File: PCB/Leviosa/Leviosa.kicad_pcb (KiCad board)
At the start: 2 copper layers, 80 x 80 mm, 26 parts, among them Q3 TIP122, Q4 TIP122, U1 LM324, U2 ATtiny13A-P, U3 TPS1H200AQDGNRQ1, U5 L7805, U6 SS495A

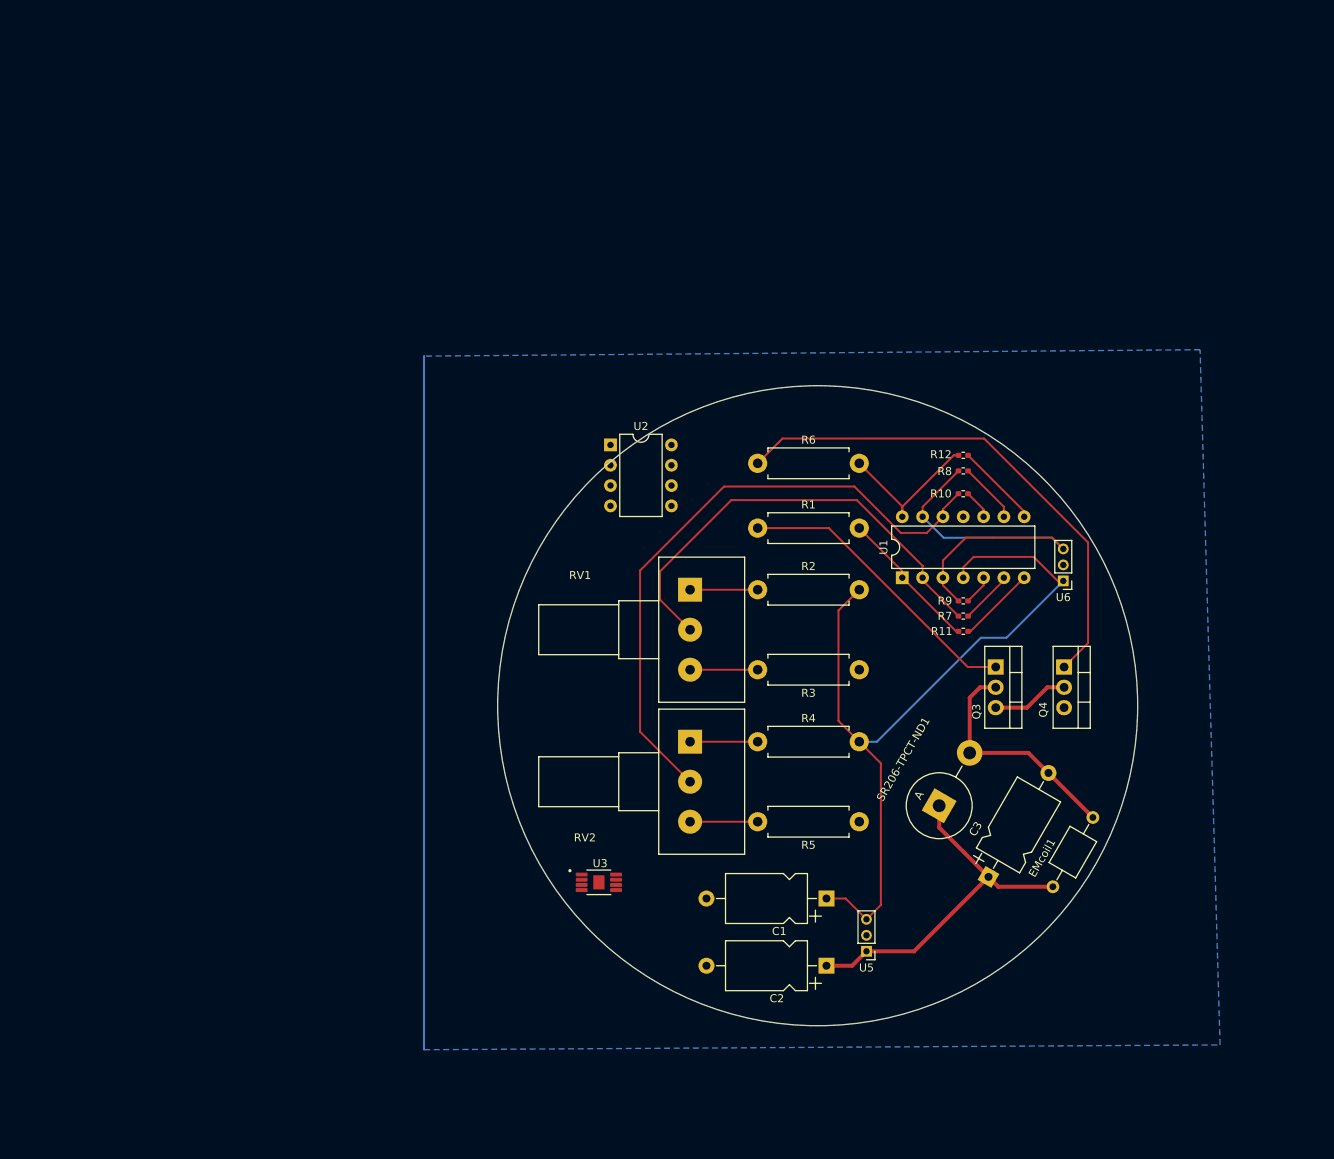
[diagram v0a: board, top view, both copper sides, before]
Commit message: update schematic footprints. PCB is sad now
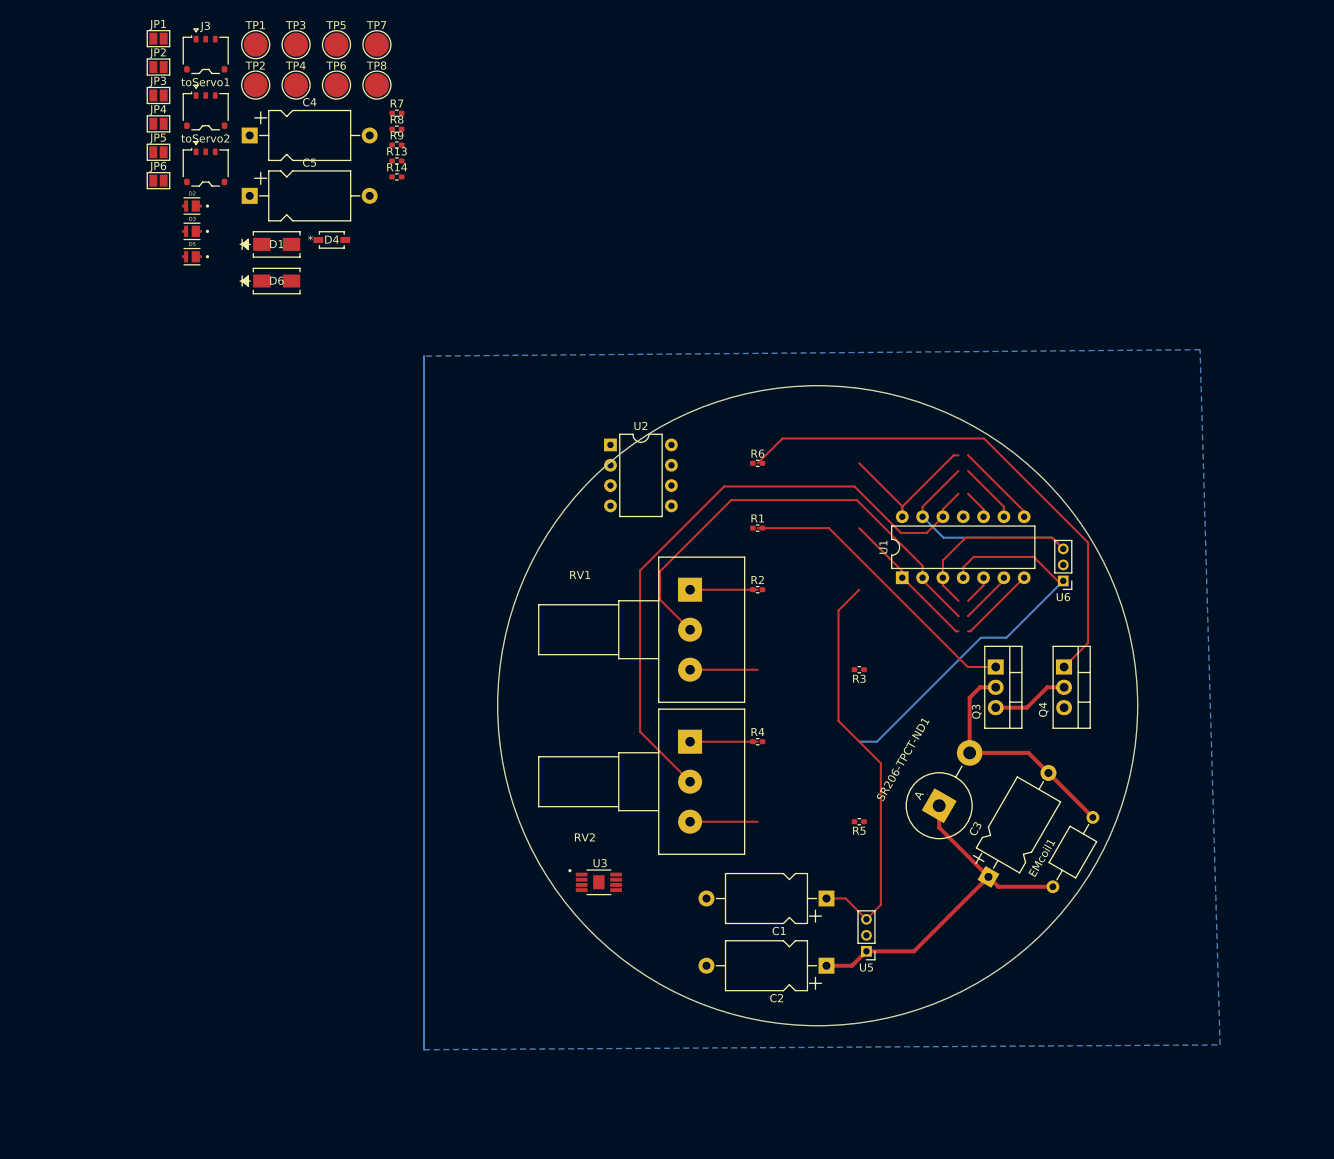
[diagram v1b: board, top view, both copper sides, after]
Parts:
- removed R10, R11, R12: DNP, Resistor_SMD:R_0402_1005Metric_Pad0.72x0.64mm_HandSolder
- added C4: 10µF, Capacitor_THT:CP_Axial_L10.0mm_D6.0mm_P15.00mm_Horizontal, F.Cu at (94.0, 42.7)
- added C5: 10µF, Capacitor_THT:CP_Axial_L10.0mm_D6.0mm_P15.00mm_Horizontal, F.Cu at (94.0, 50.3)
- added D1: D_Zener, SMAZ9V1-13-F:SMA_DIO, F.Cu at (97.4, 56.3)
- added D2: LED, MP-2016-1100-50-70:LED_MP-2016-1100-50-70, F.Cu at (86.8, 51.5)
- added D3: LED, MP-2016-1100-50-70:LED_MP-2016-1100-50-70, F.Cu at (86.8, 54.7)
- added D4: D_Zener, SZMMSZ4679T1G:SOD-123_ONS, F.Cu at (104.3, 55.8)
- added D5: LED, MP-2016-1100-50-70:LED_MP-2016-1100-50-70, F.Cu at (86.8, 57.9)
- added D6: D_Zener, SMAZ9V1-13-F:SMA_DIO, F.Cu at (97.4, 60.9)
- added J3: Conn_01x03, Connector_JST:JST_ACH_BM03B-ACHSS-GAN-ETF_1x03-1MP_P1.20mm_Vertical, F.Cu at (88.5, 32.6)
- added JP1: SolderJumper_2_Open, Jumper:SolderJumper-2_P1.3mm_Open_Pad1.0x1.5mm, F.Cu at (82.6, 30.6)
- added JP2: SolderJumper_2_Open, Jumper:SolderJumper-2_P1.3mm_Open_Pad1.0x1.5mm, F.Cu at (82.6, 34.2)
- added JP3: SolderJumper_2_Open, Jumper:SolderJumper-2_P1.3mm_Open_Pad1.0x1.5mm, F.Cu at (82.6, 37.7)
- added JP4: SolderJumper_2_Open, Jumper:SolderJumper-2_P1.3mm_Open_Pad1.0x1.5mm, F.Cu at (82.6, 41.3)
- added JP5: SolderJumper_2_Open, Jumper:SolderJumper-2_P1.3mm_Open_Pad1.0x1.5mm, F.Cu at (82.6, 44.8)
- added JP6: SolderJumper_2_Open, Jumper:SolderJumper-2_P1.3mm_Open_Pad1.0x1.5mm, F.Cu at (82.6, 48.4)
- added R13: 8kΩ, Resistor_SMD:R_0402_1005Metric_Pad0.72x0.64mm_HandSolder, F.Cu at (112.4, 45.9)
- added R14: 100kΩ, Resistor_SMD:R_0402_1005Metric_Pad0.72x0.64mm_HandSolder, F.Cu at (112.4, 47.9)
- added TP1: TestPoint, TestPoint:TestPoint_Pad_D3.0mm, F.Cu at (94.8, 31.4)
- added TP2: TestPoint, TestPoint:TestPoint_Pad_D3.0mm, F.Cu at (94.8, 36.4)
- added TP3: TestPoint, TestPoint:TestPoint_Pad_D3.0mm, F.Cu at (99.8, 31.4)
- added TP4: TestPoint, TestPoint:TestPoint_Pad_D3.0mm, F.Cu at (99.8, 36.4)
- added TP5: TestPoint, TestPoint:TestPoint_Pad_D3.0mm, F.Cu at (104.9, 31.4)
- added TP6: TestPoint, TestPoint:TestPoint_Pad_D3.0mm, F.Cu at (104.9, 36.4)
- added TP7: TestPoint, TestPoint:TestPoint_Pad_D3.0mm, F.Cu at (109.9, 31.4)
- added TP8: TestPoint, TestPoint:TestPoint_Pad_D3.0mm, F.Cu at (109.9, 36.4)
- added toServo1: Conn_01x03, Connector_JST:JST_ACH_BM03B-ACHSS-GAN-ETF_1x03-1MP_P1.20mm_Vertical, F.Cu at (88.5, 39.6)
- added toServo2: Conn_01x03, Connector_JST:JST_ACH_BM03B-ACHSS-GAN-ETF_1x03-1MP_P1.20mm_Vertical, F.Cu at (88.5, 46.6)
- C1: value 10µF -> 0.1µF
- C2: value 10µF -> 0.33µF
- R1, R4, R5, R6: footprint Resistor_THT:R_Axial_DIN0411_L9.9mm_D3.6mm_P12.70mm_Horizontal -> Resistor_SMD:R_0402_1005Metric_Pad0.72x0.64mm_HandSolder
- R2: value 200kΩ -> 100kΩ; footprint Resistor_THT:R_Axial_DIN0411_L9.9mm_D3.6mm_P12.70mm_Horizontal -> Resistor_SMD:R_0402_1005Metric_Pad0.72x0.64mm_HandSolder
- R3: value 27kΩ -> 7.8kΩ; footprint Resistor_THT:R_Axial_DIN0411_L9.9mm_D3.6mm_P12.70mm_Horizontal -> Resistor_SMD:R_0402_1005Metric_Pad0.72x0.64mm_HandSolder
- R7, R8, R9: value DNP -> 1kΩ
- moved R7 94.7 mm to (112.4, 39.9), turned to 0 degrees
- moved R9 90.9 mm to (112.4, 43.9), turned to 0 degrees
- moved R8 82.7 mm to (112.4, 41.9)
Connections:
- C3 pad 1: +12V -> /V_out
- EMcoil1 pad 1: +12V -> /V_out
- R7 pad 1: Net-(U1B--) -> Net-(D2-K)
- R7 pad 2: /set_point -> GND
- R8 pad 1: /hall_output -> Net-(D3-K)
- R8 pad 2: Net-(U1C--) -> GND
- R9 pad 1: Net-(U1B-+) -> Net-(D5-K)
- R9 pad 2: /hall_output -> GND
- RV1 pad 1: Net-(R2-Pad1) -> Net-(R3-Pad2)
- RV1 pad 3: Net-(R3-Pad2) -> Net-(R2-Pad1)
- SR206-TPCT-ND1 pad 1: +12V -> /V_out
- U1 pad 5: Net-(U1B-+) -> Net-(JP3-B)
- U1 pad 6: Net-(U1B--) -> Net-(JP4-B)
- U1 pad 9: Net-(U1C--) -> Net-(JP5-A)
- U2 pad 1: unconnected-(U2-~{RESET}/PB5-Pad1) -> Net-(J3-Pin_3)
- U2 pad 2: unconnected-(U2-PB3-Pad2) -> Net-(J3-Pin_1)
- U2 pad 3: unconnected-(U2-PB4-Pad3) -> Net-(J3-Pin_2)
- U2 pad 4: unconnected-(U2-GND-Pad4) -> GND
- U2 pad 5: unconnected-(U2-PB0-Pad5) -> Net-(U2-PB0)
- U2 pad 6: unconnected-(U2-PB1-Pad6) -> Net-(U2-PB1)
- U2 pad 7: unconnected-(U2-PB2-Pad7) -> /hall_output
- U2 pad 8: unconnected-(U2-VCC-Pad8) -> /5V
- U3 pad 1: unconnected-(U3-IN-Pad1) -> +12V
- U3 pad 2: unconnected-(U3-DIAG_EN-Pad2) -> +12V
- U3 pad 3: unconnected-(U3-~{FAULT}-Pad3) -> Net-(U3-~{FAULT})
- U3 pad 4: unconnected-(U3-CL-Pad4) -> Net-(U3-CL)
- U3 pad 5: unconnected-(U3-DELAY-Pad5) -> Net-(U3-DELAY)
- U3 pad 6: unconnected-(U3-GND-Pad6) -> GND
- U3 pad 7: unconnected-(U3-OUT-Pad7) -> /V_out
- U3 pad 8: unconnected-(U3-VS-Pad8) -> +12V
- U3 pad 9: unconnected-(U3-EP-Pad9) -> GND
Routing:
- net Net-(R3-Pad2): track 8.45 -> 0.00 mm
- net Net-(R2-Pad1): track 8.45 -> 16.9 mm
- net Net-(U1C--): track 7.58 -> 0.00 mm
- net Net-(JP5-A): track 0.00 -> 7.58 mm
- net Net-(U1B--): track 6.66 -> 0.00 mm
- net Net-(JP4-B): track 0.00 -> 6.66 mm
- net Net-(U1B-+): track 3.70 -> 0.00 mm
- net Net-(JP3-B): track 0.00 -> 3.70 mm

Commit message: update footprints and the like
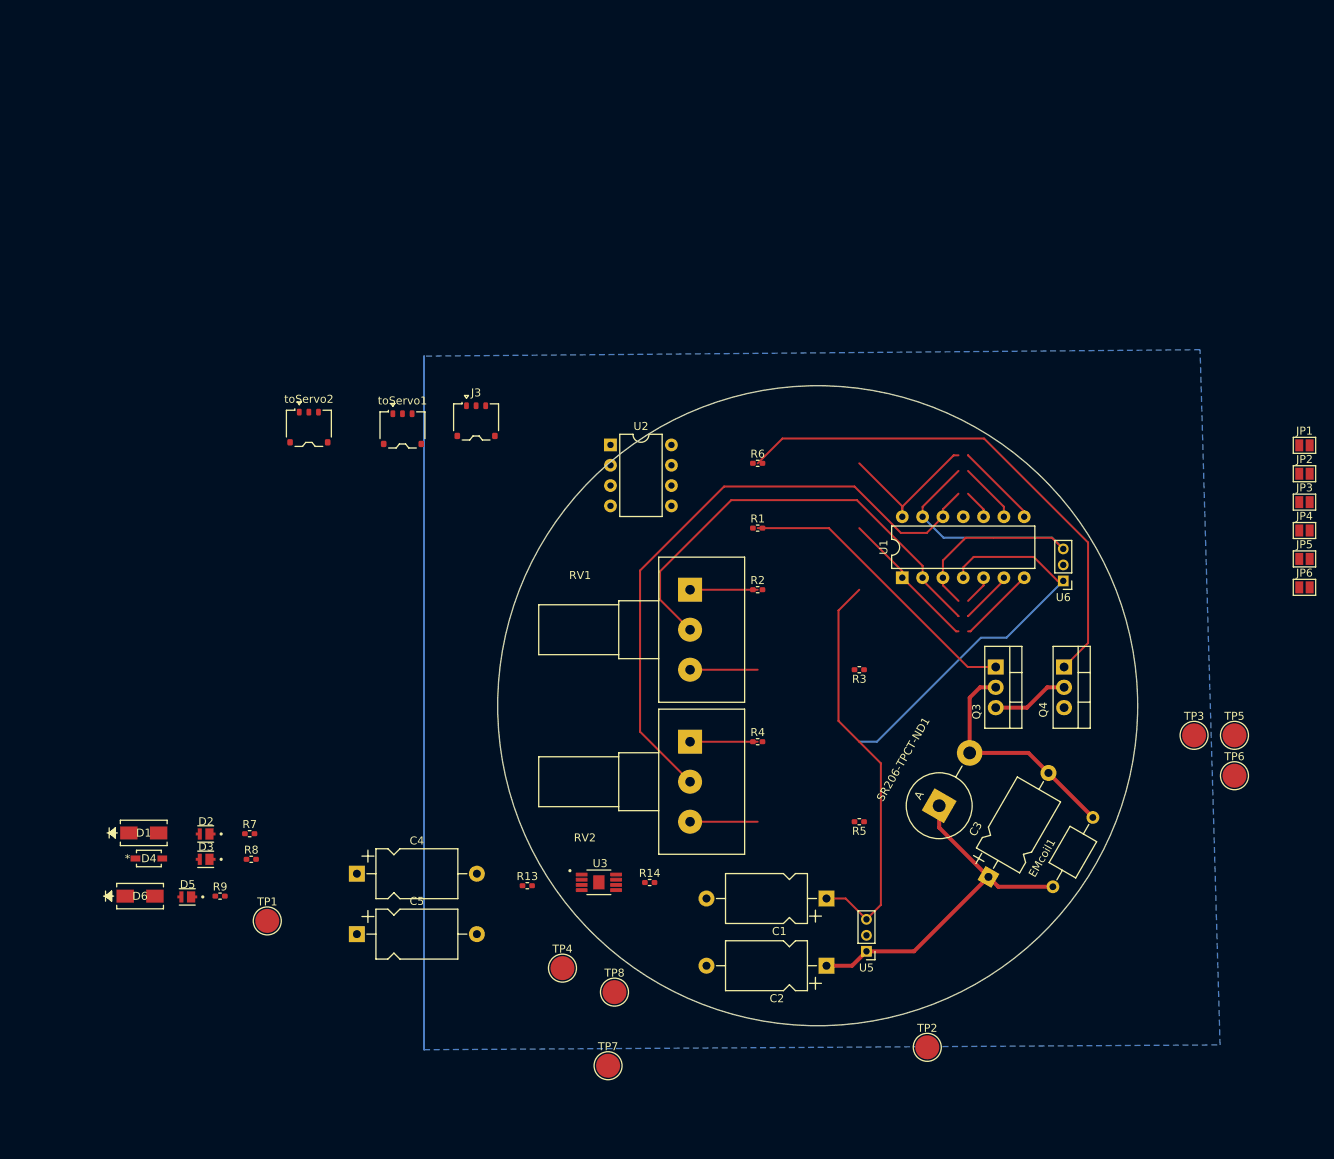
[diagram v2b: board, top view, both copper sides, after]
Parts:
- moved JP1 152.0 mm to (225.8, 81.5)
- moved JP2 152.0 mm to (225.8, 85.0)
- moved JP3 152.0 mm to (225.8, 88.5)
- moved JP4 152.0 mm to (225.8, 92.1)
- moved JP5 152.0 mm to (225.8, 95.7)
- moved JP6 152.0 mm to (225.8, 99.2)
- moved TP2 146.7 mm to (178.7, 156.7)
- moved TP3 141.6 mm to (212.1, 117.7)
- moved TP5 141.6 mm to (217.1, 117.7)
- moved TP6 141.6 mm to (217.1, 122.8)
- moved TP7 130.9 mm to (138.8, 159.0)
- moved TP8 117.2 mm to (139.6, 149.8)
- moved TP4 115.3 mm to (133.1, 146.8)
- moved TP1 109.5 mm to (96.2, 140.9)
- moved R9 96.4 mm to (90.3, 137.8)
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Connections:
- D2 pad A: (no net) -> Net-(D1-A)
- D2 pad C: (no net) -> Net-(D2-PadC)
- D3 pad A: (no net) -> Net-(D4-A)
- D3 pad C: (no net) -> Net-(D3-PadC)
- D4 pad 2: Net-(D3-A) -> Net-(D4-A)
- D5 pad A: (no net) -> Net-(D6-A)
- D5 pad C: (no net) -> Net-(D5-PadC)
- D6 pad 2: Net-(D5-A) -> Net-(D6-A)
- R7 pad 1: Net-(D2-K) -> Net-(D2-PadC)
- R8 pad 1: Net-(D3-K) -> Net-(D3-PadC)
- R9 pad 1: Net-(D5-K) -> Net-(D5-PadC)
